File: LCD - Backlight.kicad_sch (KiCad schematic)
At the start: 14 parts, among them IC2 TPS61165DBVR

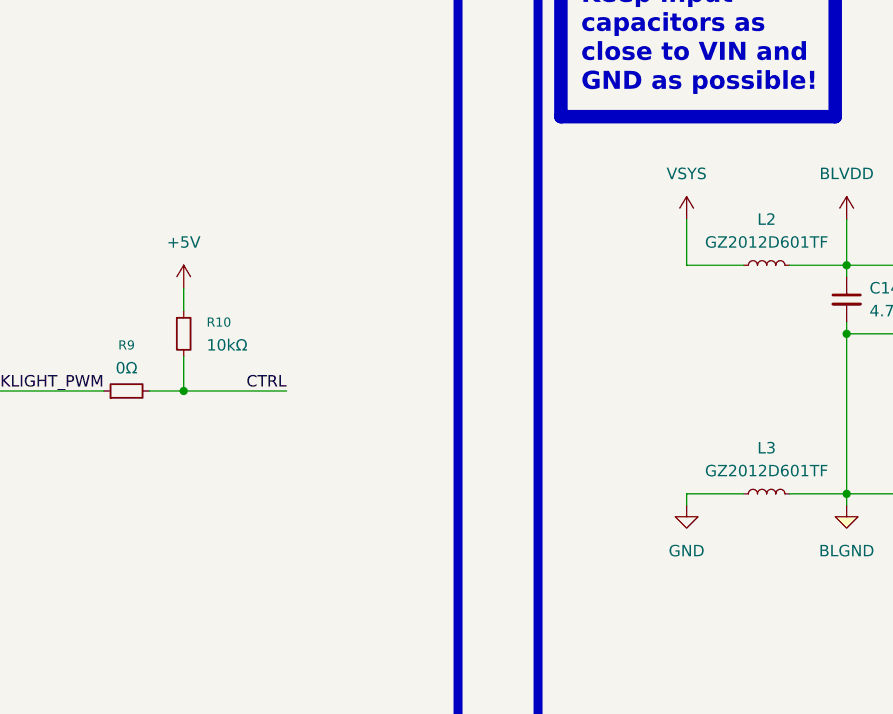
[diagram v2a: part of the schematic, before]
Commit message: added power switch, 5V and 3V3 power generation
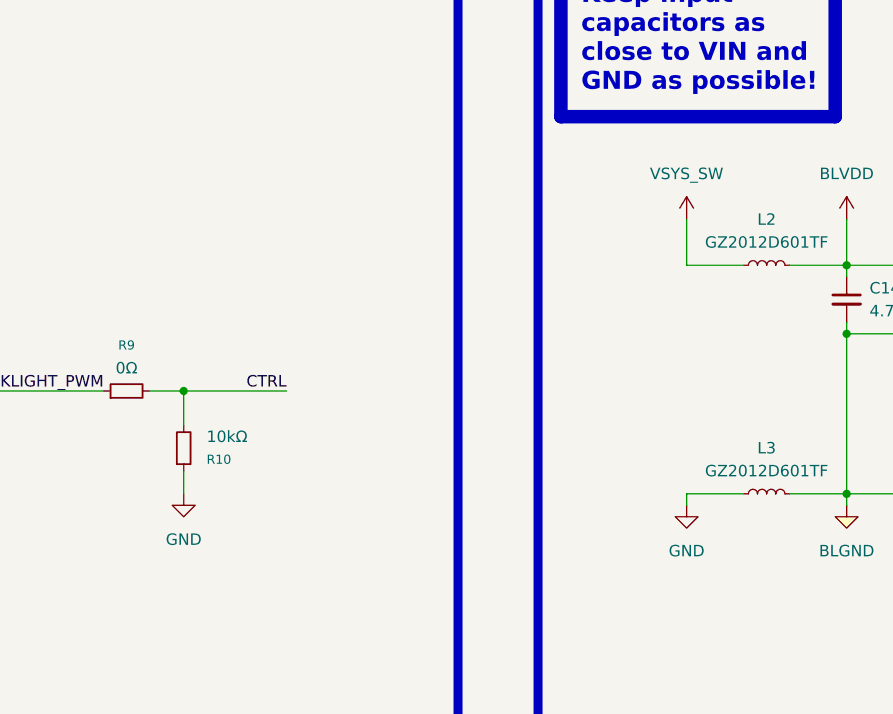
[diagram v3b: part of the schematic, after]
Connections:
- net +5V is gone; now on net GND: R10.1
- net VSYS renamed VSYS_SW
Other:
- moved on the sheet: R10
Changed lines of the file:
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@@
+	)
+	(junction
+		(at 284.48 102.87)
+		(diameter 0)
+		(color 132 0 0 1)
+	)
+	(junction
+		(at 270.51 124.46)
+		(diameter 0)
+		(color 0 0 0 0)
 	)
 	(junction
@@
 	)
 	(junction
-		(at 284.48 102.87)
-		(diameter 0)
-		(color 132 0 0 1)
-	)
-	(junction
-		(at 270.51 124.46)
-		(diameter 0)
-		(color 0 0 0 0)
-	)
-	(junction
 		(at 210.82 99.06)
 		(diameter 0)
@@
 	(wire
 		(pts
-			(xy 137.16 101.6) (xy 137.16 104.14)
+			(xy 137.16 124.46) (xy 137.16 121.92)
 		)
 		(stroke
@@
 	(wire
 		(pts
+			(xy 137.16 113.03) (xy 148.59 113.03)
+		)
+		(stroke
+			(width 0)
+			(type default)
+		)
+	)
+	(wire
+		(pts
 			(xy 284.48 109.22) (xy 284.48 110.49)
 		)
@@
 	(wire
 		(pts
-			(xy 137.16 109.22) (xy 137.16 113.03)
+			(xy 137.16 116.84) (xy 137.16 113.03)
 		)
 		(stroke
@@
 		(pts
 			(xy 276.86 124.46) (xy 289.56 124.46)
-		)
-		(stroke
-			(width 0)
-			(type default)
-		)
-	)
-	(wire
-		(pts
-			(xy 137.16 113.03) (xy 148.59 113.03)
 		)
 		(stroke
@@
 	)
 	(symbol
-		(lib_id "0_power_symbols:VSYS")
-		(at 193.04 93.98 0)
-		(unit 1)
-		(exclude_from_sim no)
-		(in_bom yes)
-		(on_board yes)
-		(dnp no)
-		(fields_autoplaced yes)
-		(property "Reference" "#PWR082"
-			(at 193.04 97.79 0)
-			(effects
-				(font
-					(size 1.27 1.27)
-				)
-				(hide yes)
-			)
-		)
-		(property "Value" "VSYS"
-			(at 193.04 88.9 0)
-			(effects
-				(font
-					(size 1.27 1.27)
-				)
-			)
-		)
-		(property "Footprint" ""
-			(at 193.04 93.98 0)
-			(effects
-				(font
-					(size 1.27 1.27)
-				)
-				(hide yes)
-			)
-		)
-		(property "Datasheet" ""
-			(at 193.04 93.98 0)
-			(effects
-				(font
-					(size 1.27 1.27)
-				)
-				(hide yes)
-			)
-		)
-		(property "Description" "Power symbol creates a global label with name \"VSYS\""
-			(at 193.04 93.98 0)
-			(effects
-				(font
-					(size 1.27 1.27)
-				)
-				(hide yes)
-			)
-		)
-		(pin "1"
-		)
-		(instances
-			(project ""
-				(path "/0650c7a8-acba-429c-9f8e-eec0baf0bc1c/fede4c36-00cc-4d3d-b71c-5243ba232202/d532fde6-fcc8-4703-b00a-b5308b206554"
-					(reference "#PWR082")
-					(unit 1)
-				)
-			)
-		)
-	)
-	(symbol
 		(lib_id "0_resistors:0603WAF100KT5E")
 		(at 276.86 115.57 0)
@@
 	)
 	(symbol
+		(lib_id "power:GND")
+		(at 137.16 124.46 0)
+		(unit 1)
+		(exclude_from_sim no)
+		(in_bom yes)
+		(on_board yes)
+		(dnp no)
+		(fields_autoplaced yes)
+		(property "Reference" "#PWR025"
+			(at 137.16 130.81 0)
+			(effects
+				(font
+					(size 1.27 1.27)
+				)
+				(hide yes)
+			)
+		)
+		(property "Value" "GND"
+			(at 137.16 129.54 0)
+			(effects
+				(font
+					(size 1.27 1.27)
+				)
+			)
+		)
+		(property "Footprint" ""
+			(at 137.16 124.46 0)
+			(effects
+				(font
+					(size 1.27 1.27)
+				)
+				(hide yes)
+			)
+		)
+		(property "Datasheet" ""
+			(at 137.16 124.46 0)
+			(effects
+				(font
+					(size 1.27 1.27)
+				)
+				(hide yes)
+			)
+		)
+		(property "Description" "Power symbol creates a global label with name \"GND\" , ground"
+			(at 137.16 124.46 0)
+			(effects
+				(font
+					(size 1.27 1.27)
+				)
+				(hide yes)
+			)
+		)
+		(pin "1"
+		)
+		(instances
+			(project "transmitter"
+				(path "/0650c7a8-acba-429c-9f8e-eec0baf0bc1c/fede4c36-00cc-4d3d-b71c-5243ba232202/d532fde6-fcc8-4703-b00a-b5308b206554"
+					(reference "#PWR025")
+					(unit 1)
+				)
+			)
+		)
+	)
+	(symbol
 		(lib_id "0_resistors:0402WGF1002TCE")
-		(at 137.16 106.68 0)
+		(at 137.16 119.38 0)
+		(mirror x)
 		(unit 1)
 		(exclude_from_sim no)
@@
 		(fields_autoplaced yes)
 		(property "Reference" "R10"
-			(at 139.7 105.41 0)
+			(at 139.7 120.65 0)
 			(effects
 				(font
@@
 		)
 		(property "Value" "10kΩ"
-			(at 139.7 107.95 0)
+			(at 139.7 118.11 0)
 			(effects
 				(font
@@
 		)
 		(property "Footprint" "0_resistors:R_0402_1005Metric"
-			(at 137.16 106.68 0)
+			(at 137.16 119.38 0)
 			(effects
 				(font
@@
 		)
 		(property "Datasheet" "~"
-			(at 137.16 106.68 0)
+			(at 137.16 119.38 0)
 			(effects
 				(font
@@
 		)
 		(property "Description" "Resistor, small symbol"
-			(at 137.16 106.68 0)
+			(at 137.16 119.38 0)
 			(effects
 				(font
@@
 		)
 		(property "Supplier 1" "JLCPCB"
-			(at 137.16 106.68 0)
+			(at 137.16 119.38 0)
 			(effects
 				(font
@@
 		)
 		(property "Supplier Part Number 1" "C25744"
-			(at 137.16 106.68 0)
+			(at 137.16 119.38 0)
 			(effects
 				(font
@@
 	)
 	(symbol
-		(lib_id "power:+5V")
-		(at 137.16 101.6 0)
-		(unit 1)
-		(exclude_from_sim no)
-		(in_bom yes)
-		(on_board yes)
-		(dnp no)
-		(fields_autoplaced yes)
-		(property "Reference" "#PWR025"
-			(at 137.16 105.41 0)
-			(effects
-				(font
-					(size 1.27 1.27)
-				)
-				(hide yes)
-			)
-		)
-		(property "Value" "+5V"
-			(at 137.16 96.52 0)
-			(effects
-				(font
-					(size 1.27 1.27)
-				)
-			)
-		)
-		(property "Footprint" ""
-			(at 137.16 101.6 0)
-			(effects
-				(font
-					(size 1.27 1.27)
-				)
-				(hide yes)
-			)
-		)
-		(property "Datasheet" ""
-			(at 137.16 101.6 0)
-			(effects
-				(font
-					(size 1.27 1.27)
-				)
-				(hide yes)
-			)
-		)
-		(property "Description" "Power symbol creates a global label with name \"+5V\""
-			(at 137.16 101.6 0)
-			(effects
-				(font
-					(size 1.27 1.27)
-				)
-				(hide yes)
-			)
-		)
-		(pin "1"
-		)
-		(instances
-			(project ""
-				(path "/0650c7a8-acba-429c-9f8e-eec0baf0bc1c/fede4c36-00cc-4d3d-b71c-5243ba232202/d532fde6-fcc8-4703-b00a-b5308b206554"
-					(reference "#PWR025")
-					(unit 1)
-				)
-			)
-		)
-	)
-	(symbol
 		(lib_id "0_capacitors:CL05B224KO5NNNC")
 		(at 237.49 113.03 0)
@@
 					(unit 1)
 				)
+			)
+		)
+	)
+	(symbol
+		(lib_id "0_power_symbols:VSYS_SW")
+		(at 193.04 93.98 0)
+		(unit 1)
+		(exclude_from_sim no)
+		(in_bom yes)
+		(on_board yes)
+		(dnp no)
+		(fields_autoplaced yes)
+		(property "Reference" "#PWR082"
+			(at 193.04 97.79 0)
+			(effects
+				(font
+					(size 1.27 1.27)
+				)
+				(hide yes)
+			)
+		)
+		(property "Value" "VSYS_SW"
+			(at 193.04 88.9 0)
+			(effects
+				(font
+					(size 1.27 1.27)
+				)
+			)
+		)
+		(property "Footprint" ""
+			(at 193.04 93.98 0)
+			(effects
+				(font
+					(size 1.27 1.27)
+				)
+				(hide yes)
+			)
+		)
+		(property "Datasheet" ""
+			(at 193.04 93.98 0)
+			(effects
+				(font
+					(size 1.27 1.27)
+				)
+				(hide yes)
+			)
+		)
+		(property "Description" "Power symbol creates a global label with name \"VSYS_SW\""
+			(at 193.04 93.98 0)
+			(effects
+				(font
+					(size 1.27 1.27)
+				)
+				(hide yes)
+			)
+		)
+		(pin "1"
+		)
+		(instances
+			(project "transmitter"
+				(path "/0650c7a8-acba-429c-9f8e-eec0baf0bc1c/fede4c36-00cc-4d3d-b71c-5243ba232202/d532fde6-fcc8-4703-b00a-b5308b206554"
+					(reference "#PWR082")
+					(unit 1)
+				)
